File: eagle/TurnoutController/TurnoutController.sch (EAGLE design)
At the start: 15 parts, among them IC1 L293D, J1 POWER_JACKPTH

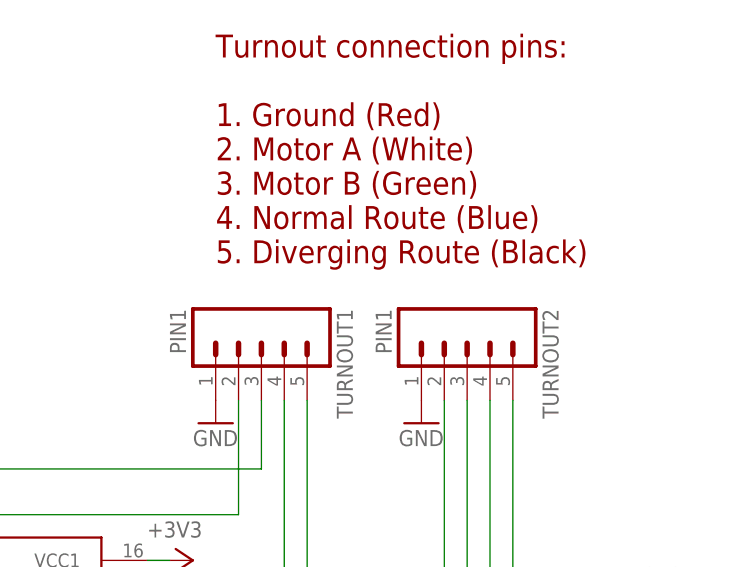
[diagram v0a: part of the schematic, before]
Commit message: 1.  Cleanup continues.  BlockController and the corresponding controller are deprecated along with SignalController and it's controller board.  These are replaced by the InputModule and OutputModule respectively 2.  TurnoutHandler moved to the MultiModuleController project folder 3.  Module moved to the MultiModuleController project folder 4.  More database cleanup work completed.
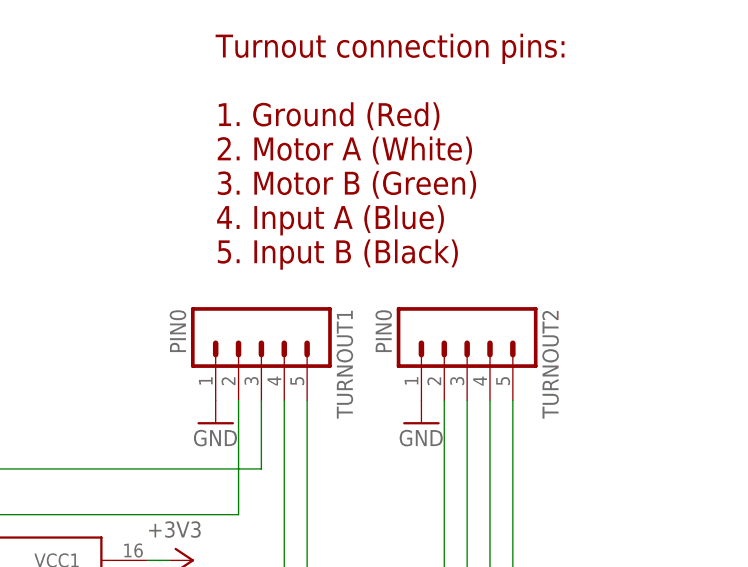
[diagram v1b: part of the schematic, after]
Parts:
- TURNOUT1, TURNOUT2: value PIN1 -> PIN0
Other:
- note added: "Turnout connection pins: 1. Ground (Red) 2. Motor A (White) 3. Motor B (Green) 4. Input A (Blue) 5. Input B (Black)"
- note removed: "Turnout connection pins: 1. Ground (Red) 2. Motor A (White) 3. Motor B (Green) 4. Normal Route (Blue) 5. Diverging Route (Black)"
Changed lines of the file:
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@@
 </classes>
 <parts>
-<part name="TURNOUT1" library="con-amp-quick" deviceset="M05" device="" value="PIN1"/>
+<part name="TURNOUT1" library="con-amp-quick" deviceset="M05" device="" value="PIN0"/>
 <part name="GND6" library="SparkFun-Aesthetics" deviceset="GND" device=""/>
 <part name="R15" library="SparkFun-Resistors" deviceset="RESISTOR" device="PTH-1/4W" value="3.3K"/>
@@
 <part name="GND9" library="SparkFun-Aesthetics" deviceset="GND" device=""/>
 <part name="GND11" library="SparkFun-Aesthetics" deviceset="GND" device=""/>
-<part name="TURNOUT2" library="con-amp-quick" deviceset="M05" device="" value="PIN1"/>
+<part name="TURNOUT2" library="con-amp-quick" deviceset="M05" device="" value="PIN0"/>
 <part name="IC1" library="st-microelectronics" deviceset="L293D" device=""/>
 <part name="GND12" library="SparkFun-Aesthetics" deviceset="GND" device=""/>
@@
 2. Motor A (White)
 3. Motor B (Green)
-4. Normal Route (Blue)
-5. Diverging Route (Black)</text>
+4. Input A (Blue)
+5. Input B (Black)</text>
 </plain>
 <instances>
